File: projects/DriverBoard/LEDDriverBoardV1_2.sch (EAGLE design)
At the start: 93 parts

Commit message: began updating flash panel V6.2
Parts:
- added V1: (no value), BrownSpaceEngineering:VIA-120MIL
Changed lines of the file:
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@@
 <part name="R2" library="CNTRL_BOARD" deviceset="RESISTOR" device="" value="1M"/>
 <part name="R3" library="CNTRL_BOARD" deviceset="RESISTOR" device="" value="1M"/>
+<part name="V1" library="BrownSpaceEngineering" deviceset="VIA" device="-120MIL"/>
 </parts>
 <sheets>
@@
 <instance part="M3" gate="G$1" x="109.22" y="109.22"/>
 <instance part="M4" gate="G$1" x="320.04" y="109.22"/>
+<instance part="V1" gate="G$1" x="154.94" y="30.48"/>
 </instances>
 <busses>

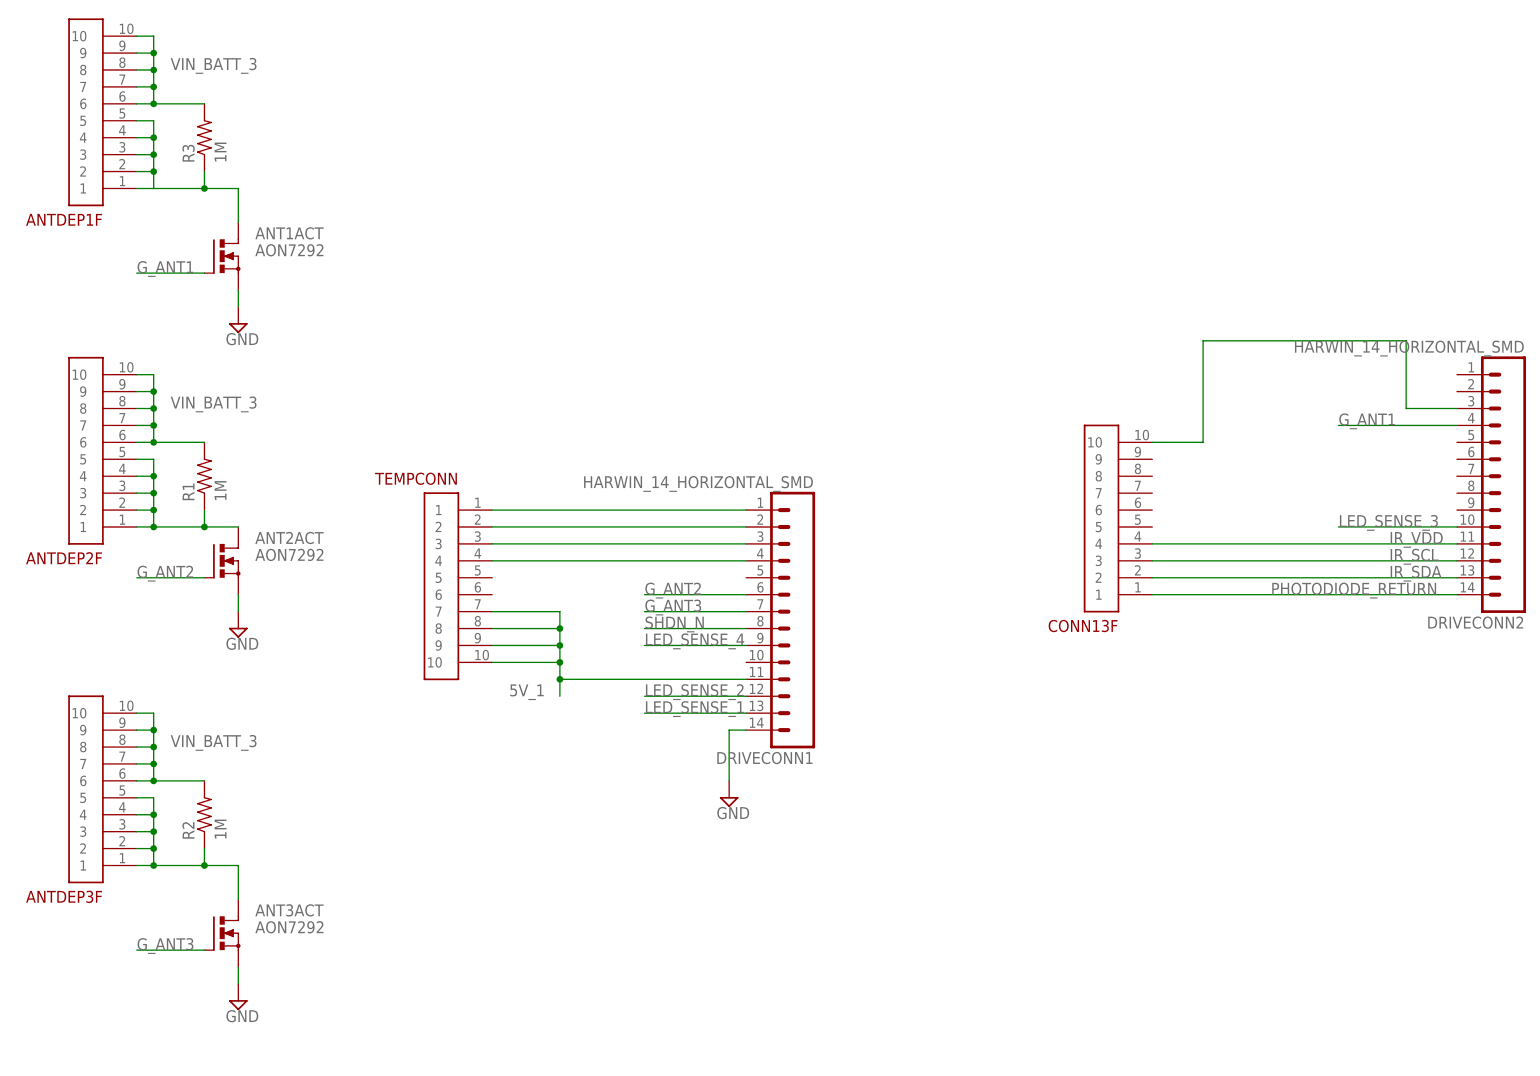
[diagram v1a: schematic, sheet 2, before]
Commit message: Updates to Radio Adapter Board, Driver Board, Flash Panel. Somebody forgot to commit for a whole week or so....
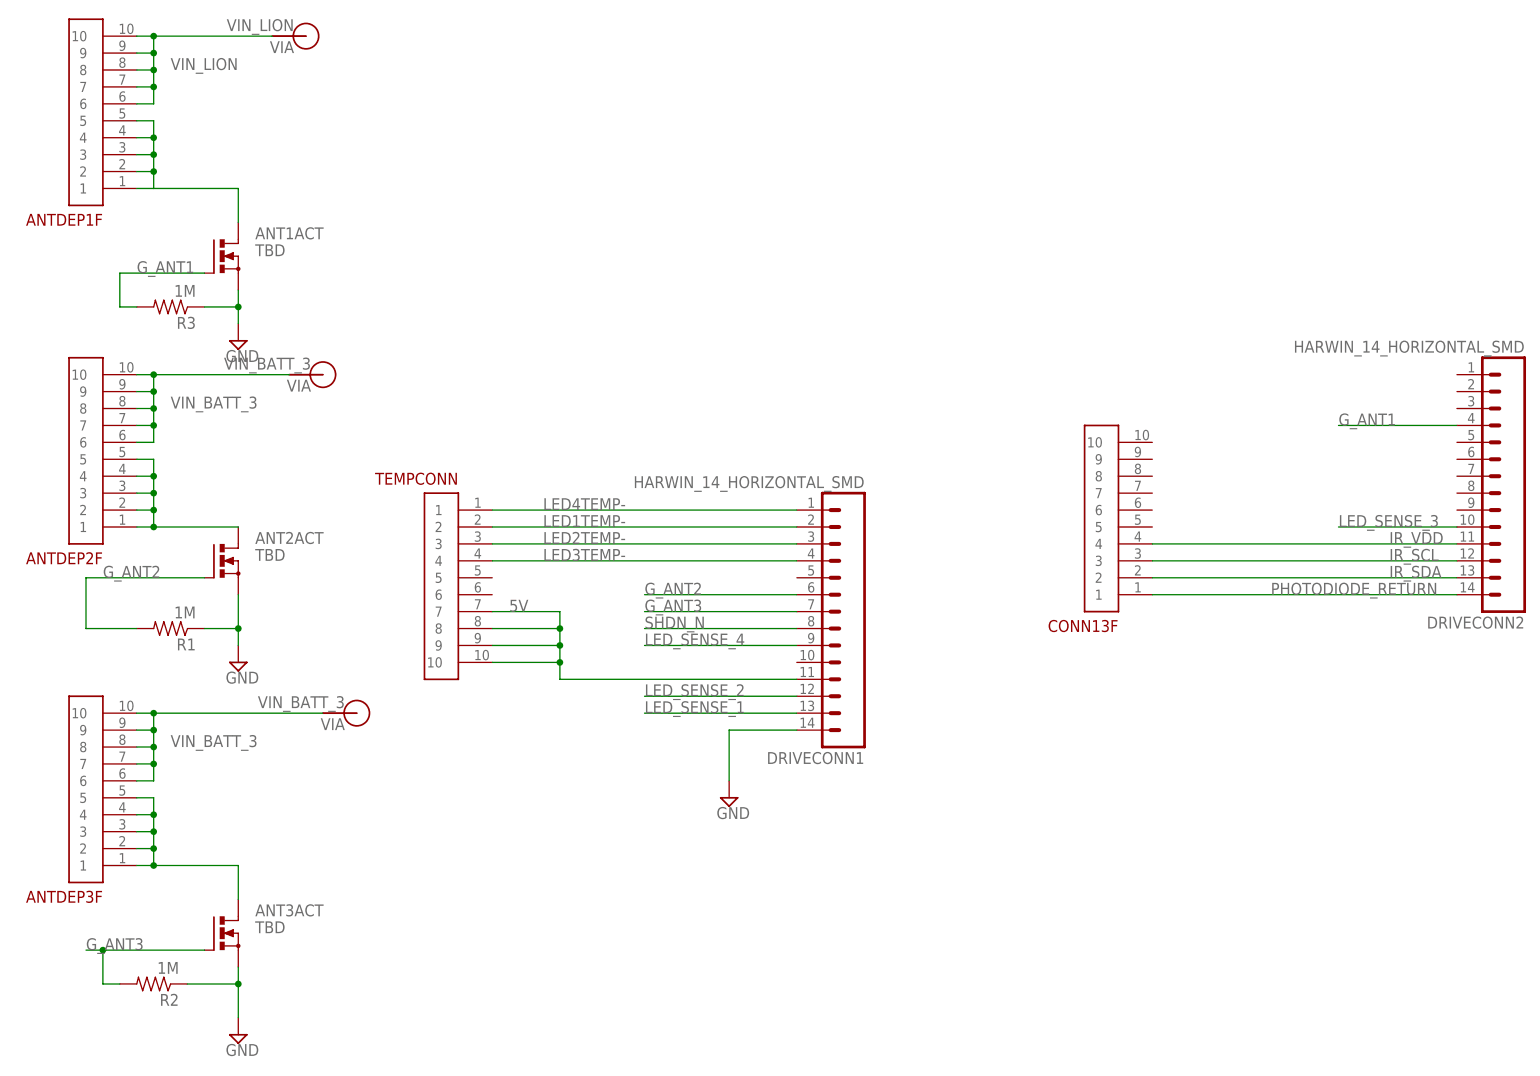
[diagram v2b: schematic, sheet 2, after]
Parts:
- removed GND_BATT, VIN_BATT_1, VIN_BATT_3: (no value), wirepad:3,81/1,4
- added V2, V3: VIN_BATT_3, BrownSpaceEngineering:VIA-120MIL
- added V4: VIN_LION, BrownSpaceEngineering:VIA-120MIL
- added V5: GND, BrownSpaceEngineering:VIA-120MIL
- added V6, V7: VIN_BATT_1, BrownSpaceEngineering:VIA-120MIL
- ANT1ACT, ANT2ACT, ANT3ACT: value AON7292 -> TBD
- V1: value (none) -> GND
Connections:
- net 5V_1 renamed 5V
- net N$8 renamed LED3TEMP-
- removed net N$17: CONN13F.10, DRIVECONN2.3
- new net VIN_LION: ANTDEP1F.10, ANTDEP1F.6, ANTDEP1F.7, ANTDEP1F.8, ANTDEP1F.9, V4.P$1
- net GND: now also R1.1, R2.1, R3.1, V1.P$1, V5.P$1; no longer GND_BATT.P
- net G_ANT1: now also R3.2
- net G_ANT2: now also R1.2
- net G_ANT3: now also R2.2
- net N$20: no longer R2.1
- net N$21: no longer R1.1
- net N$22: no longer R3.1
- net VIN_BATT_1: now also V6.P$1, V7.P$1; no longer VIN_BATT_1.P
- net VIN_BATT_3: now also V2.P$1, V3.P$1; no longer ANTDEP1F.10, ANTDEP1F.6, ANTDEP1F.7, ANTDEP1F.8, ANTDEP1F.9, R1.2, R2.2, R3.2, VIN_BATT_3.P
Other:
- moved on the sheet: DRIVECONN1, R1, R2, R3, VOUT_1

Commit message: Removed txt document and some continued Flash and Driver board updates.
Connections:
- new net DEP_RTN1: TEMPCONN.6
- new net DEP_RTN2: CONN13F.6
- new net DEP_SEND: CONN13F.5, TEMPCONN.5
- net GND: now also CONN13F.10
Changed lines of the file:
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@@
 <pinref part="SUPPLY17" gate="GND" pin="GND"/>
+</segment>
+<segment>
+<pinref part="CONN13F" gate="G$1" pin="10"/>
+<wire x1="195.58" y1="96.52" x2="203.2" y2="96.52" width="0.1524" layer="91"/>
+<label x="198.12" y="96.52" size="1.778" layer="95"/>
 </segment>
 </net>
@@
 </segment>
 </net>
+<net name="DEP_SEND" class="0">
+<segment>
+<pinref part="CONN13F" gate="G$1" pin="5"/>
+<wire x1="195.58" y1="83.82" x2="203.2" y2="83.82" width="0.1524" layer="91"/>
+<label x="198.12" y="83.82" size="1.778" layer="95"/>
+</segment>
+<segment>
+<pinref part="TEMPCONN" gate="G$1" pin="5"/>
+<wire x1="96.52" y1="76.2" x2="106.68" y2="76.2" width="0.1524" layer="91"/>
+<label x="99.06" y="76.2" size="1.778" layer="95"/>
+</segment>
+</net>
+<net name="DEP_RTN2" class="0">
+<segment>
+<pinref part="CONN13F" gate="G$1" pin="6"/>
+<wire x1="195.58" y1="86.36" x2="203.2" y2="86.36" width="0.1524" layer="91"/>
+<label x="198.12" y="86.36" size="1.778" layer="95"/>
+</segment>
+</net>
+<net name="DEP_RTN1" class="0">
+<segment>
+<pinref part="TEMPCONN" gate="G$1" pin="6"/>
+<wire x1="96.52" y1="73.66" x2="106.68" y2="73.66" width="0.1524" layer="91"/>
+<label x="99.06" y="73.66" size="1.778" layer="95"/>
+</segment>
+</net>

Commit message: Completed all changes to Flash Panel and Driver Board. Additional library changes and additions for antenna deployment detection circuitry.
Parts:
- removed CONN13F: (no value), LED_Driver_Board:M50-3120545
- removed DRIVECONN1, DRIVECONN2: HARWIN_14_HORIZONTAL_SMD, LED_Driver_Board:M80-5321442
- added J1, J2: M80-53210, BrownSpaceEngineering:M80-53210
- added P13: (no value), LED_Driver_Board:M50-3120545
- added V8: SHDN_N, BrownSpaceEngineering:VIA60MIL-SQ
- added V9: GND, BrownSpaceEngineering:VIA60MIL-SQ
- RSHDN: device resistor:R-US_R0603 -> BrownSpaceEngineering:RES0805
- V2, V3: value VIN_BATT_3 -> VIN_LIFE1
- V6, V7: value VIN_BATT_1 -> VIN_LIFE3
- renumbered ANT1ACT to M5, ANT2ACT to M6, ANT3ACT to M7, ANTDEP1F to ANTDEP1, ANTDEP2F to ANTDEP2, ANTDEP3F to ANTDEP3, TEMPCONN to P12
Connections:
- net VIN_BATT_1 renamed VIN_LIFE3
- net VIN_BATT_3 renamed VIN_LIFE1
- removed net DEP_RTN1: P12.6
- removed net DEP_RTN2: CONN13F.6
- removed net DEP_SEND: CONN13F.5, P12.5
- removed net G_ANT1: DRIVECONN2.4, M5.G, R3.2
- removed net G_ANT2: DRIVECONN1.6, M6.G, R1.2
- removed net G_ANT3: DRIVECONN1.7, M7.G, R2.2
- removed net PHOTODIODE_RETURN: CONN13F.1, DRIVECONN2.14
- new net ANT_DRV1: J2.P$1, M5.G, R3.2
- new net ANT_DRV2: J2.P$10, M6.G, R1.2
- new net ANT_DRV3: J1.P$5, M7.G, R2.2
- new net DET_RTN: J2.P$2, P13.5
- new net PD_RTN: J2.P$6, P13.1
- net 5V: now also J1.P$7; no longer DRIVECONN1.11
- net GND: now also J1.P$6, J2.P$7, P12.5, P13.10, V9.P$1; no longer CONN13F.10, DRIVECONN1.14
- net IR_SCL: now also J2.P$4, P13.3; no longer CONN13F.3, DRIVECONN2.12
- net IR_SDA: now also J2.P$5, P13.2; no longer CONN13F.2, DRIVECONN2.13
- net IR_VDD: now also J2.P$3, P13.4; no longer CONN13F.4, DRIVECONN2.11
- net LED1TEMP-: now also J1.P$3, P12.3; no longer DRIVECONN1.2, P12.2
- net LED2TEMP-: now also J1.P$4, P12.4; no longer DRIVECONN1.3, P12.3
- net LED3TEMP-: now also J1.P$1, P12.1; no longer DRIVECONN1.4, P12.4
- net LED4TEMP-: now also J1.P$2, P12.2; no longer DRIVECONN1.1, P12.1
- net LED_SENSE_1: now also J1.P$10; no longer DRIVECONN1.13
- net LED_SENSE_2: now also J1.P$9; no longer DRIVECONN1.12
- net LED_SENSE_3: now also J2.P$9; no longer DRIVECONN2.10
- net LED_SENSE_4: now also J1.P$8; no longer DRIVECONN1.9
- net SHDN_N: now also J2.P$8, V8.P$1; no longer DRIVECONN1.8
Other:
- note added: "NC"
